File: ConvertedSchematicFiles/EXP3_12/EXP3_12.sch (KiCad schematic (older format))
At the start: 7 parts

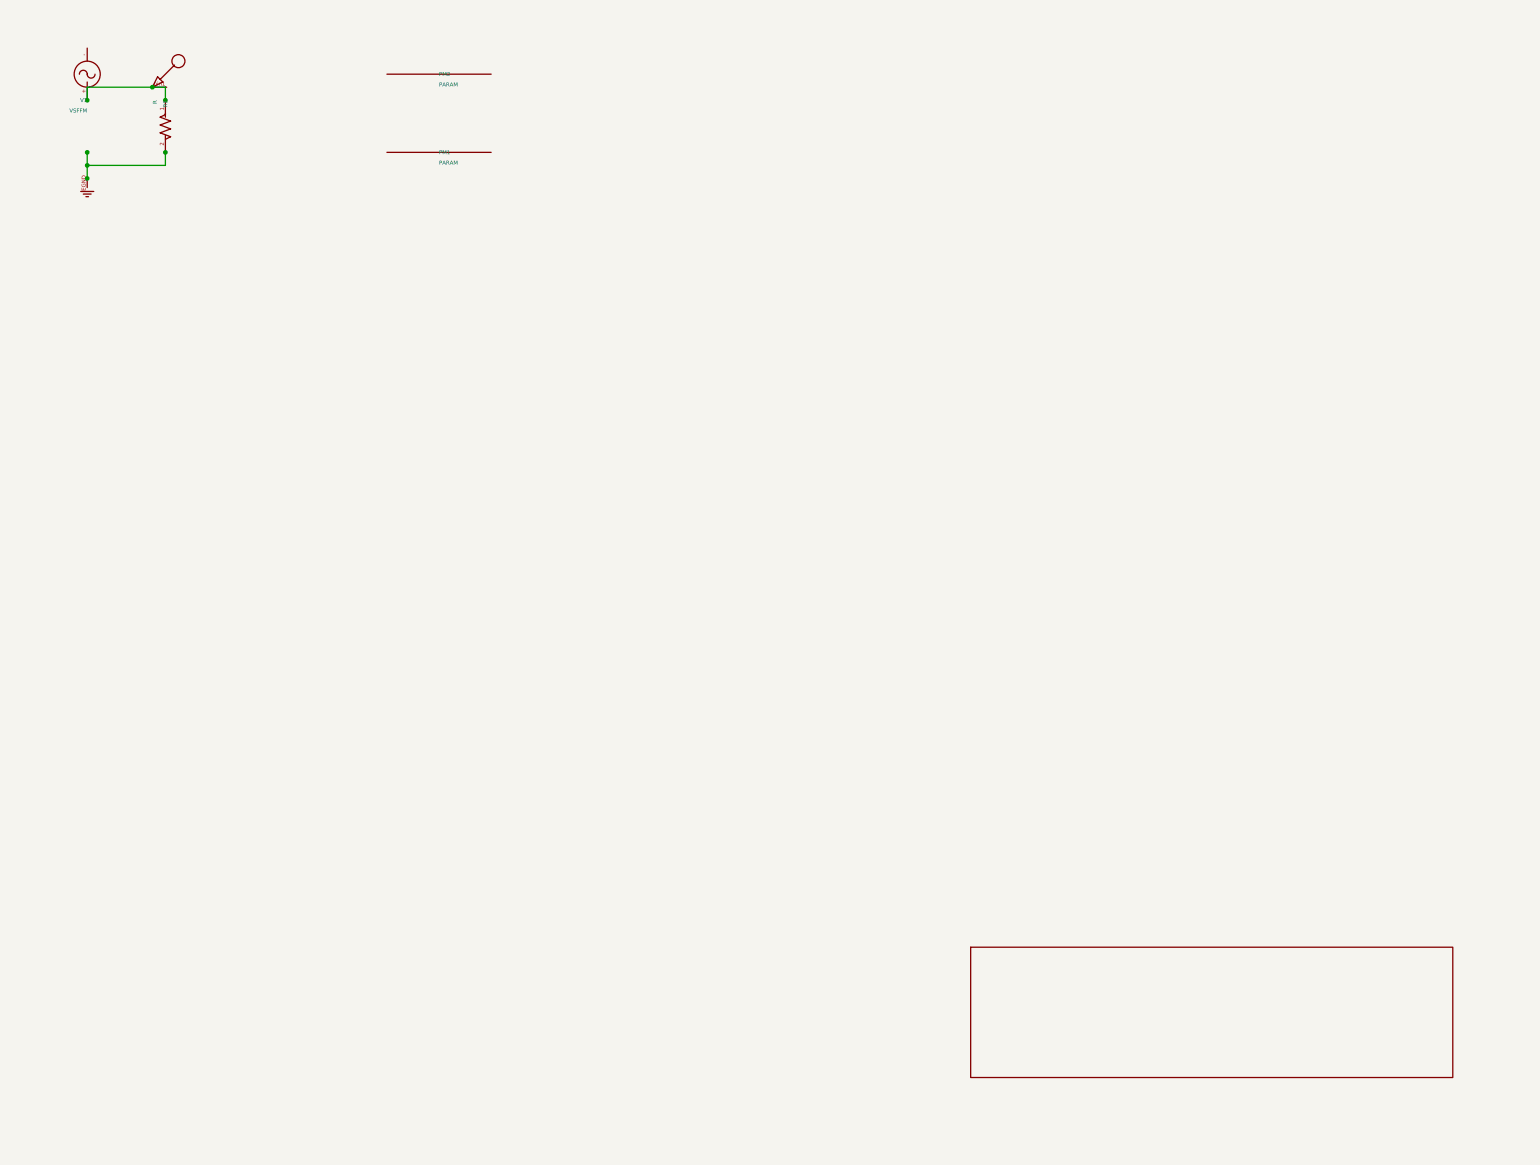
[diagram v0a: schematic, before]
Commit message: Excluded some components. These no longer appear after conversion. When calling shell commands, filenames are in "quotes"
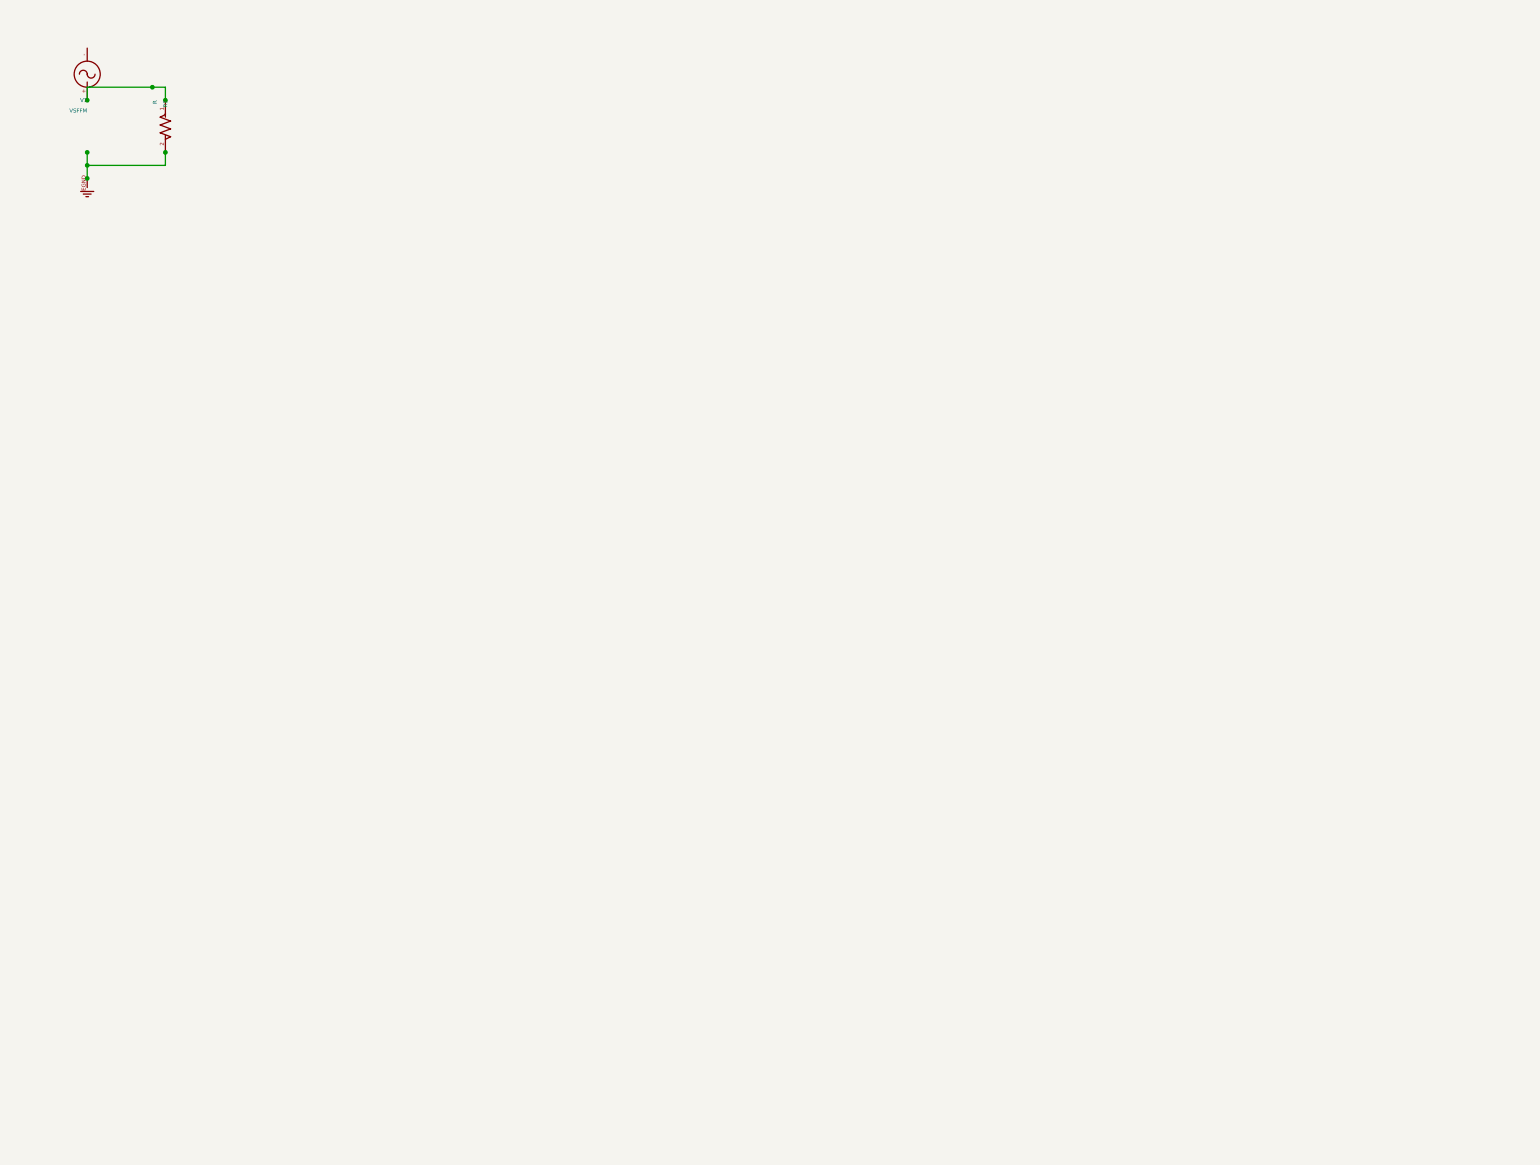
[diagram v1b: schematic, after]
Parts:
- removed PM1, PM2: PARAM, symbol PARAM_PSPICE
- removed nodeMarker: nodeMarker, symbol NODEMARKER_PSPICE
- removed titleblk: titleblk, symbol TITLEBLK_PSPICE
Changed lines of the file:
@@
 	-1    0    0    1
-$EndComp
-$Comp
-L PARAM_PSPICE PM2
-U 1 1 14636915
-P 4100 700
-F 0 "PM2" H 4100 700 30  0000 L CNN
-F 1 "PARAM" H 4100 780 30  0000 L CNN
-	1    4100 700
-	1    0    0    1
-$EndComp
-$Comp
-L PARAM_PSPICE PM1
-U 1 1 77747793
-P 4100 1300
-F 0 "PM1" H 4100 1300 30  0000 L CNN
-F 1 "PARAM" H 4100 1380 30  0000 L CNN
-	1    4100 1300
-	1    0    0    1
-$EndComp
-$Comp
-L TITLEBLK_PSPICE titleblk
-U 1 1 74238335
-P 11880 8400
-F 0 "titleblk" H 23760 16800 30  0001 L CNN
-F 1 "titleblk" H 23760 16880 30  0001 L CNN
-	1    11880 8400
-	1    0    0    1
-$EndComp
-$Comp
-L NODEMARKER_PSPICE nodeMarker
-U 1 1 99885386
-P 1900 800
-F 0 "nodeMarker" H 3800 1600 30  0001 L CNN
-F 1 "nodeMarker" H 3800 1680 30  0001 L CNN
-	1    1900 800
-	1    0    0    1
 $EndComp
 Wire Wire Line

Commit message: Ports issue fixed. Now annotation for ports is #PWR? function added "itos"
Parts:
- removed EGND: EGND, symbol EGND_PSPICE
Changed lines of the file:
@@
 $EndDescr
 $Comp
-L EGND_PSPICE EGND
+L EGND_PSPICE #PWR1
 U 1 1 14289383
 P 1400 1500
-F 0 "EGND" H 2800 3000 30  0001 L CNN
+F 0 "#PWR1" H 2800 3000 30  0001 L CNN
 F 1 "EGND" H 2800 3080 30  0001 L CNN
 	1    1400 1500

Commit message: Added LICENSE.txt
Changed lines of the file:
@@
 $EndDescr
 $Comp
-L EGND_PSPICE #PWR1
+L GND #PWR1
 U 1 1 14289383
 P 1400 1500

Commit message: Orientation fix. Library components are now inverted, with +ve y axis going up. In Schematic files, +ve y axis is downwards. This is how the KiCad libraries are. As a result of the above fixed, the converted GND is now oriented correctly.
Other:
- moved on the sheet: V1
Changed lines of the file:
@@
 F 1 "EGND" H 2800 3080 30  0001 L CNN
 	1    1400 1500
-	1    0    0    1
+	1    0    0    -1
 $EndComp
 $Comp
@@
 F 1 "R" H 2000 980 30  0000 L CNN
 	1    2000 900
-	0    -1    1    0
+	0    1    1    0
 $EndComp
 $Comp
@@
 F 1 "VSFFM" H 1400 980 30  0000 L CNN
 	1    1400 900
-	-1    0    0    1
+	-1    0    0    -1
 $EndComp
 Wire Wire Line

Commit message: Removed the use of exec, wrote basename function, made integration with eSim easier.
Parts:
- added PM1, PM2: PARAM, symbol PARAM_PSPICE
- added nodeMarker: nodeMarker, symbol nodeMarker_PSPICE
- added titleblk: titleblk, symbol titleblk_PSPICE
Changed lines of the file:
@@
-EESchema Schematic File Version 2  date Wednesday 08 March 2000 03:01:09 AM IST
+EESchema Schematic File Version 2  date
 LIBS:power
 LIBS:device
@@
 LIBS:contrib
 LIBS:valves
-LIBS:ConvertedSchematicFiles/EXP3_12-cache
 EELAYER 25  0
 EELAYER END
@@
 Sheet 1 1
 Title ""
-Date "08 Mar 2000"
+Date ""
 Rev ""
 Comp ""
@@
 	-1    0    0    -1
 $EndComp
+$Comp
+L PARAM_PSPICE PM2
+U 1 1 14636915
+P 4100 700
+F 0 "PM2" H 4100 700 30  0000 L CNN
+F 1 "PARAM" H 4100 780 30  0000 L CNN
+	1    4100 700
+	1    0    0    -1
+$EndComp
+$Comp
+L PARAM_PSPICE PM1
+U 1 1 77747793
+P 4100 1300
+F 0 "PM1" H 4100 1300 30  0000 L CNN
+F 1 "PARAM" H 4100 1380 30  0000 L CNN
+	1    4100 1300
+	1    0    0    -1
+$EndComp
+$Comp
+L titleblk_PSPICE titleblk
+U 1 1 74238335
+P 11880 8400
+F 0 "titleblk" H 23760 16800 30  0001 L CNN
+F 1 "titleblk" H 23760 16880 30  0001 L CNN
+	1    11880 8400
+	1    0    0    -1
+$EndComp
+$Comp
+L nodeMarker_PSPICE nodeMarker
+U 1 1 99885386
+P 1900 800
+F 0 "nodeMarker" H 3800 1600 30  0001 L CNN
+F 1 "nodeMarker" H 3800 1680 30  0001 L CNN
+	1    1900 800
+	1    0    0    -1
+$EndComp
 Wire Wire Line
